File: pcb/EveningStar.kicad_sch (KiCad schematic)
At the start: 20 parts, among them J1 Conn_01x03_Pin, Q1 IRLL014NTRPBF, U1 74HC132, U2 ISO6721RBD

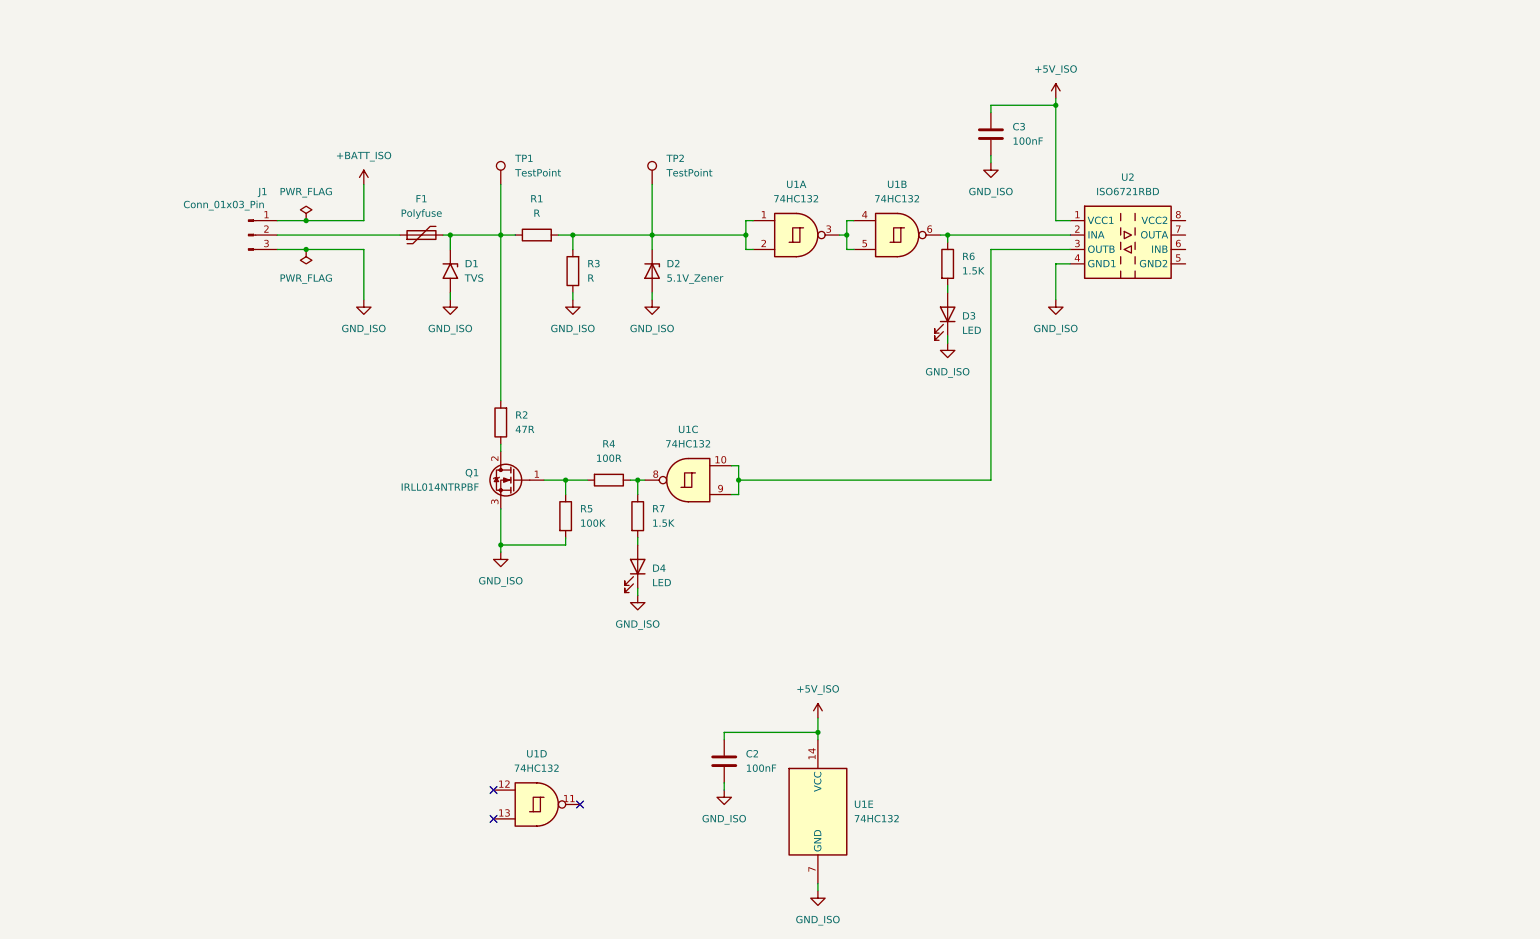
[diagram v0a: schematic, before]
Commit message: feat: implement more of the meterbus side isolated circuit
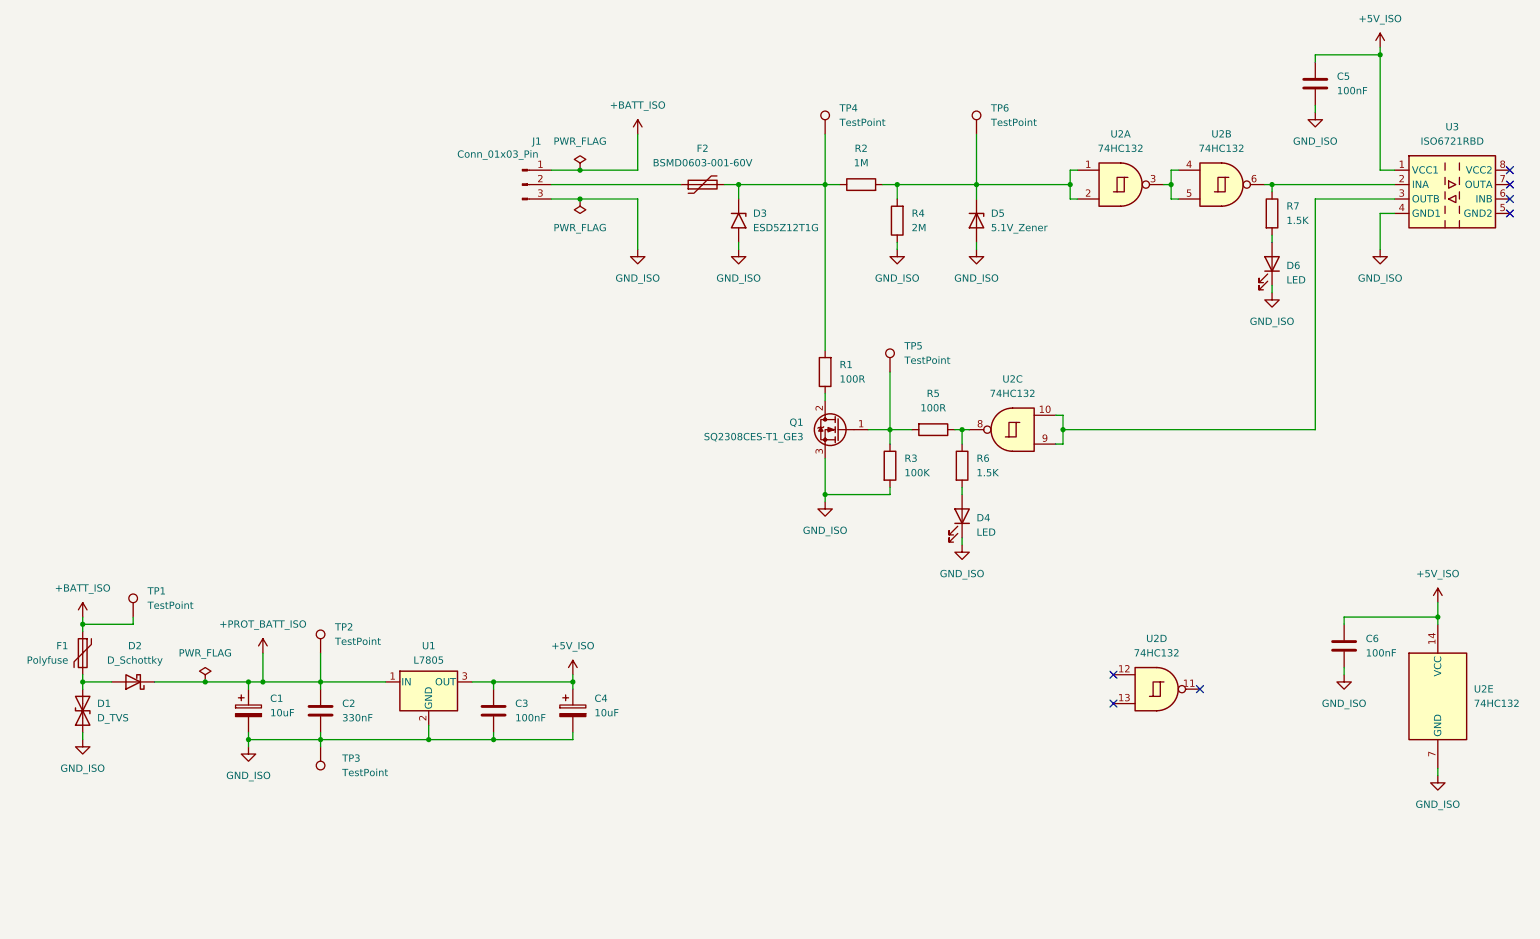
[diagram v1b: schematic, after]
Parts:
- added C1, C4: 10uF, symbol Device:C_Polarized
- added C2: 330nF, symbol Device:C
- added C3: 100nF, symbol Device:C
- added D1: D_TVS, symbol Device:D_TVS
- added D2: D_Schottky, symbol Device:D_Schottky
- added F1: Polyfuse, symbol Device:Polyfuse
- added TP1, TP2, TP3, TP5: TestPoint, symbol Connector:TestPoint
- added U1: L7805, symbol Regulator_Linear:L7805
- D3: renamed from D1; value TVS -> ESD5Z12T1G; footprint Diode_SMD:D_SMB -> Diode_SMD:D_SOD-523
- F2: renamed from F1; value Polyfuse -> BSMD0603-001-60V; footprint (none) -> Fuse:Fuse_0603_1608Metric_Pad1.05x0.95mm_HandSolder
- Q1: value IRLL014NTRPBF -> SQ2308CES-T1_GE3; footprint Package_TO_SOT_SMD:SOT-223-3_TabPin2 -> Package_TO_SOT_SMD:SOT-23
- R1: renamed from R2; value 47R -> 100R
- R2: renamed from R1; value R -> 1M
- R4: renamed from R3; value R -> 2M
- renumbered C3 to C5, C2 to C6, D2 to D5, D3 to D6, R5 to R3, R4 to R5, R7 to R6, R6 to R7, TP1 to TP4, TP2 to TP6, U1 to U2, U2 to U3
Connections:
- net +5V_ISO: now also C3.1, C4.1, U1.3 (OUT)
- net +BATT_ISO: now also F1.1, TP1.1
- net GND_ISO: now also C1.2, C2.2, C3.2, C4.2, D1.1 (A1), TP3.1, U1.2 (GND)
- net at Q1.1 (G), R3.1, R5.2: now also TP5.1
- new net: D1.2 (A2), D2.2 (A), F1.2
- new net +PROT_BATT_ISO: C1.1, C2.1, D2.1 (K), TP2.1, U1.1 (IN)
- no-connect marks 3 -> 7
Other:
- moved on the sheet: C5, C6, D3, D4, D5, D6, F2, J1, Q1, R1, R2, R3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

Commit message: feat: add 3.3V PSU
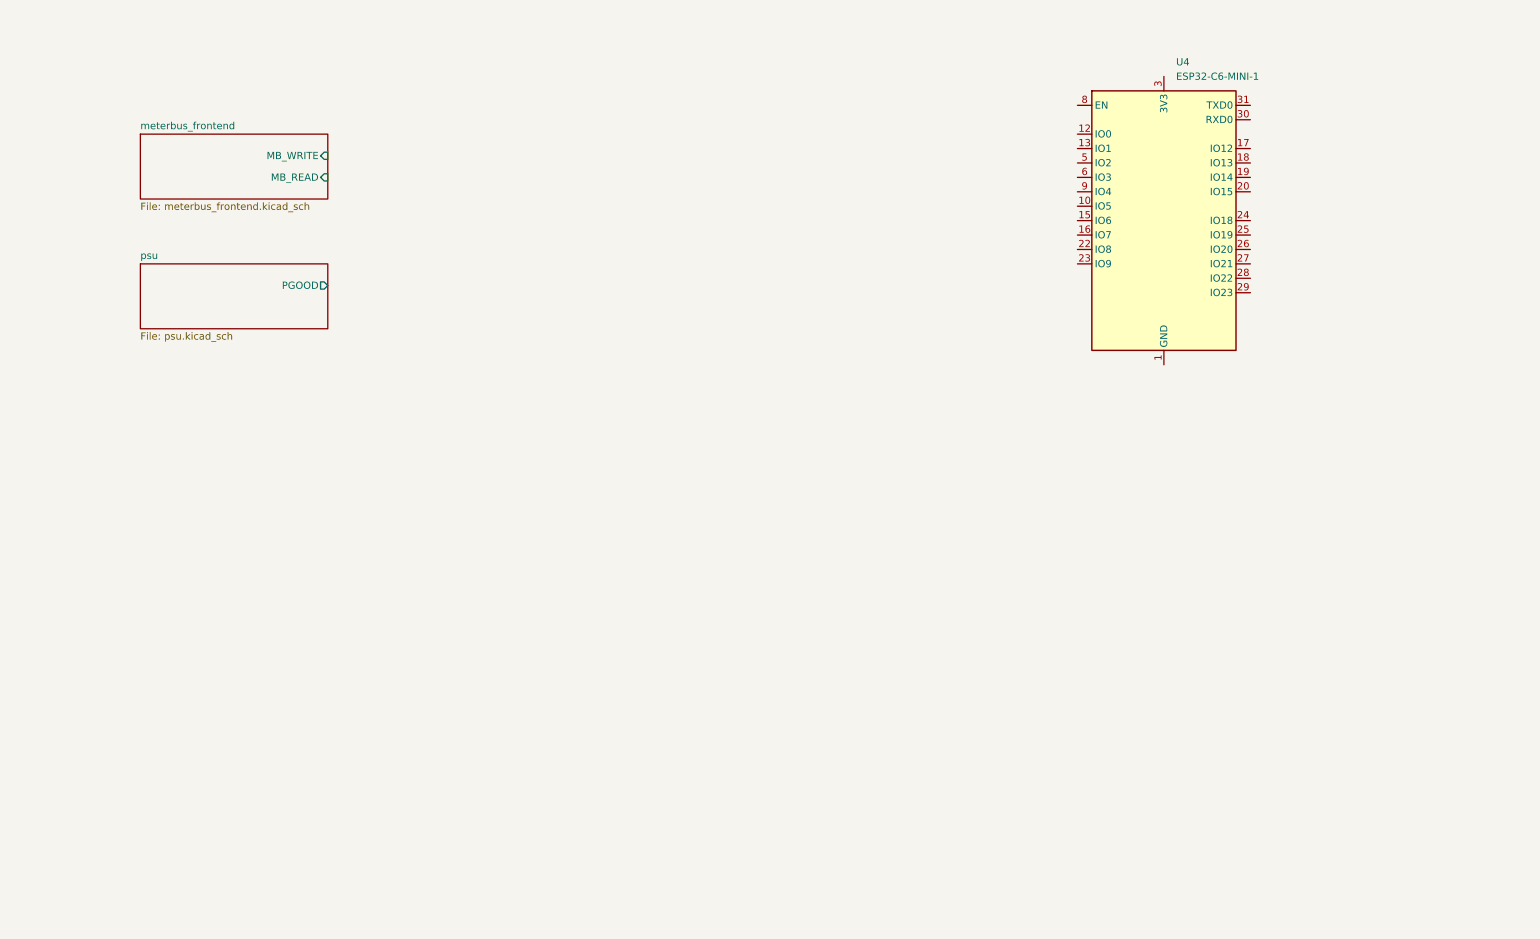
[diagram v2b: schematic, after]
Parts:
- removed C1, C4: 10uF, symbol Device:C_Polarized
- removed C2: 330nF, symbol Device:C
- removed C3, C5, C6: 100nF, symbol Device:C
- removed D1: D_TVS, symbol Device:D_TVS
- removed D2: D_Schottky, symbol Device:D_Schottky
- removed D3: ESD5Z12T1G, Diode_SMD:D_SOD-523, symbol Diode:SM6T15A
- removed D4, D6: LED, symbol Device:LED
- removed D5: 5.1V_Zener, symbol Device:D_Zener
- removed F1: Polyfuse, symbol Device:Polyfuse
- removed F2: BSMD0603-001-60V, Fuse:Fuse_0603_1608Metric_Pad1.05x0.95mm_HandSolder, symbol Device:Polyfuse
- removed J1: Conn_01x03_Pin, symbol Connector:Conn_01x03_Pin
- removed Q1: SQ2308CES-T1_GE3, Package_TO_SOT_SMD:SOT-23, symbol custom_symbols:IRLL014NTRPBF
- removed R1, R5: 100R, symbol Device:R
- removed R2: 1M, symbol Device:R
- removed R3: 100K, symbol Device:R
- removed R4: 2M, symbol Device:R
- removed R6, R7: 1.5K, symbol Device:R
- removed TP1, TP2, TP3, TP4, TP5, TP6: TestPoint, symbol Connector:TestPoint
- removed U1: L7805, symbol Regulator_Linear:L7805
- removed U2: 74HC132, symbol custom_symbols:74HC132
- removed U3: ISO6721RBD, Package_SO:SOIC-8_3.9x4.9mm_P1.27mm, symbol Isolator:ISO6721RBD
- added U4: ESP32-C6-MINI-1, RF_Module:ESP32-C6-MINI-1, symbol RF_Module:ESP32-C6-MINI-1
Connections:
- new net: U4.1 (GND), U4.11 (GND), U4.14 (GND), U4.2 (GND), U4.36 (GND), U4.37 (GND), U4.38 (GND), U4.39 (GND), U4.40 (GND), U4.41 (GND), U4.42 (GND), U4.43 (GND), U4.44 (GND), U4.45 (GND), U4.46 (GND), U4.47 (GND), U4.48 (GND), U4.49 (GND), U4.50 (GND), U4.51 (GND), U4.52 (GND), U4.53 (GND)
- no-connect marks 7 -> 0
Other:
- added sheet meterbus_frontend (meterbus_frontend.kicad_sch)
- added sheet psu (psu.kicad_sch)

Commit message: feat: add MCU sheet with USB, reset and programming circuitry
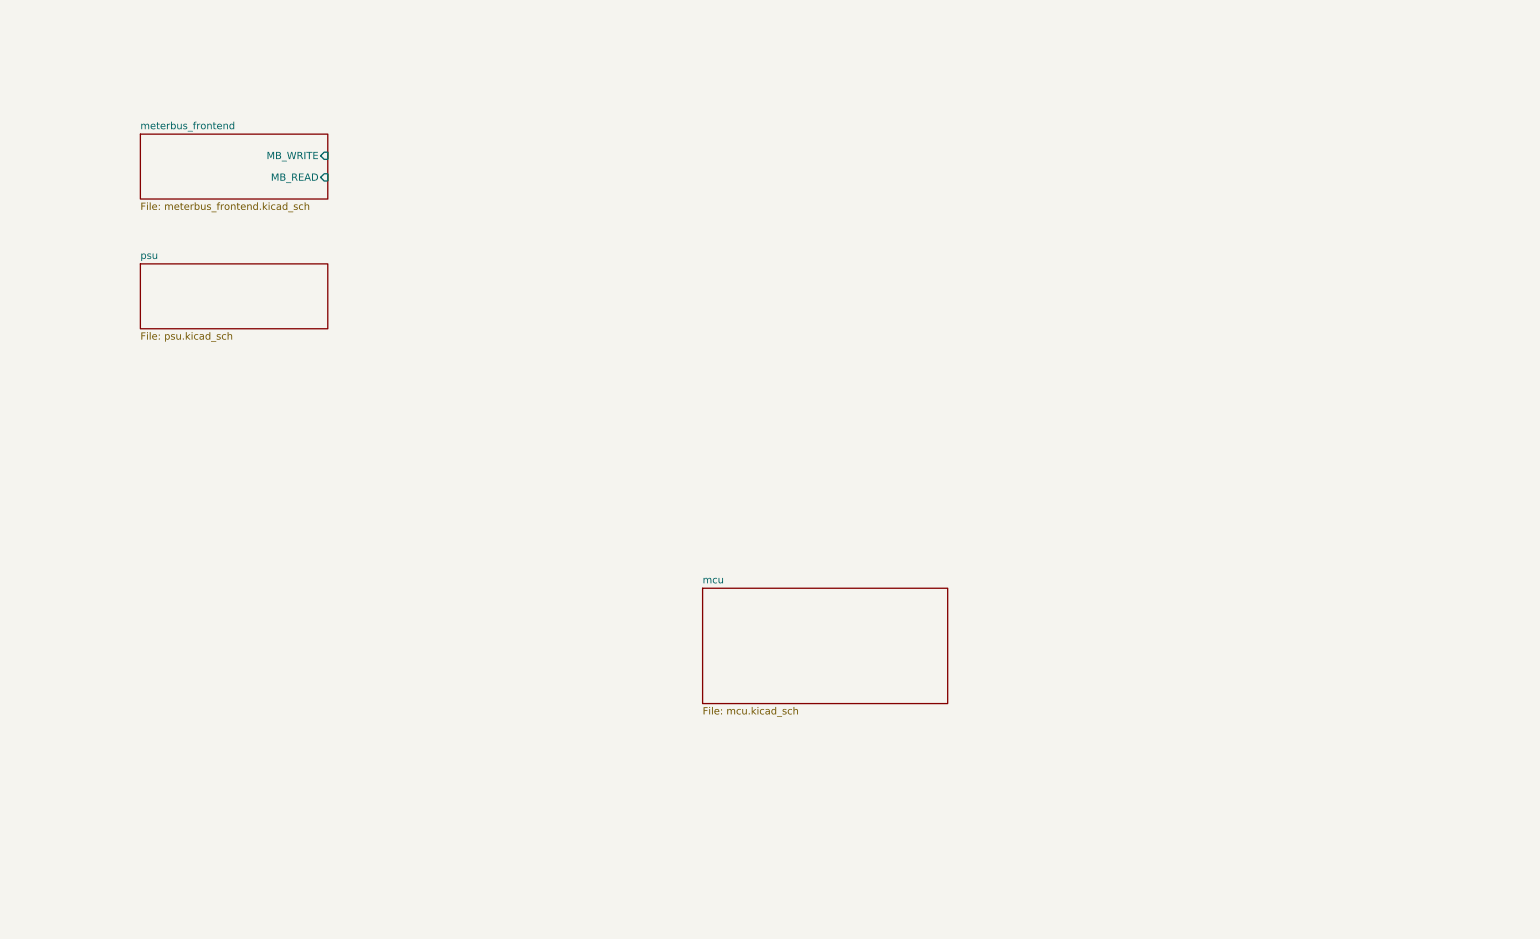
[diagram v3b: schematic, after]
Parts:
- removed U4: ESP32-C6-MINI-1, RF_Module:ESP32-C6-MINI-1, symbol RF_Module:ESP32-C6-MINI-1
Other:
- added sheet mcu (mcu.kicad_sch)
- sheet psu ports: added none; removed PGOOD
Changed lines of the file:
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@@
 	(generator_version "10.0")
 	(paper "A4")
-	(symbol
-		(lib_id "RF_Module:ESP32-C6-MINI-1")
-		(at 215.9 52.07 0)
-		(unit 1)
-		(body_style 1)
-		(exclude_from_sim no)
-		(in_bom yes)
-		(on_board yes)
-		(in_pos_files yes)
-		(dnp no)
-		(fields_autoplaced yes)
-		(property "Reference" "U4"
-			(at 218.0433 24.13 0)
-			(show_name no)
-			(do_not_autoplace no)
-			(effects
-				(font
-					(size 1.27 1.27)
-				)
-				(justify left)
-			)
-		)
-		(property "Value" "ESP32-C6-MINI-1"
-			(at 218.0433 26.67 0)
-			(show_name no)
-			(do_not_autoplace no)
-			(effects
-				(font
-					(size 1.27 1.27)
-				)
-				(justify left)
-			)
-		)
-		(property "Footprint" "RF_Module:ESP32-C6-MINI-1"
-			(at 233.68 77.47 0)
-			(hide yes)
-			(show_name no)
-			(do_not_autoplace no)
-			(effects
-				(font
-					(size 1.27 1.27)
-				)
-			)
-		)
-		(property "Datasheet" "https://www.espressif.com/sites/default/files/documentation/esp32-c6-mini-1_mini-1u_datasheet_en.pdf"
-			(at 215.9 15.24 0)
-			(hide yes)
-			(show_name no)
-			(do_not_autoplace no)
-			(effects
-				(font
-					(size 1.27 1.27)
-				)
-			)
-		)
-		(property "Description" "RF Module, ESP32-C6 SoC, Wi-Fi 802.11b/g/n/ax, Bluetooth, BLE, Zigbee, Thread, 32-bit, 3.3V, SMD, onboard antenna"
-			(at 215.9 12.7 0)
-			(hide yes)
-			(show_name no)
-			(do_not_autoplace no)
-			(effects
-				(font
-					(size 1.27 1.27)
-				)
-			)
-		)
-		(pin "35"
-		)
-		(pin "38"
-		)
-		(pin "10"
-		)
-		(pin "24"
-		)
-		(pin "27"
-		)
-		(pin "25"
-		)
-		(pin "28"
-		)
-		(pin "26"
-		)
-		(pin "30"
-		)
-		(pin "23"
-		)
-		(pin "44"
-		)
-		(pin "47"
-		)
-		(pin "14"
-		)
-		(pin "7"
-		)
-		(pin "15"
-		)
-		(pin "9"
-		)
-		(pin "11"
-		)
-		(pin "19"
-		)
-		(pin "50"
-		)
-		(pin "42"
-		)
-		(pin "40"
-		)
-		(pin "45"
-		)
-		(pin "29"
-		)
-		(pin "52"
-		)
-		(pin "43"
-		)
-		(pin "48"
-		)
-		(pin "46"
-		)
-		(pin "34"
-		)
-		(pin "49"
-		)
-		(pin "20"
-		)
-		(pin "53"
-		)
-		(pin "36"
-		)
-		(pin "51"
-		)
-		(pin "39"
-		)
-		(pin "37"
-		)
-		(pin "18"
-		)
-		(pin "21"
-		)
-		(pin "22"
-		)
-		(pin "41"
-		)
-		(pin "8"
-		)
-		(pin "16"
-		)
-		(pin "12"
-		)
-		(pin "13"
-		)
-		(pin "32"
-		)
-		(pin "17"
-		)
-		(pin "33"
-		)
-		(pin "31"
-		)
-		(pin "1"
-		)
-		(pin "6"
-		)
-		(pin "5"
-		)
-		(pin "4"
-		)
-		(pin "3"
-		)
-		(pin "2"
-		)
-		(instances
-			(project "EveningStar"
-				(path "/4c61f5a2-f8d4-462a-9bc3-d74437d30372"
-					(reference "U4")
-					(unit 1)
-				)
-			)
-		)
-	)
 	(sheet
 		(at 35.56 36.83)
@@
 			)
 		)
-		(pin "PGOOD" output
-			(at 68.58 63.5 0)
-			(effects
-				(font
-					(size 1.27 1.27)
-				)
-				(justify right)
-			)
-		)
 		(instances
 			(project "EveningStar"
@@
 				)
 			)
+		)
+	)
+	(sheet
+		(at 134.62 116.84)
+		(size 43.18 20.32)
+		(exclude_from_sim no)
+		(in_bom yes)
+		(on_board yes)
+		(dnp no)
+		(fields_autoplaced yes)
+		(stroke
+			(width 0.1524)
+			(type solid)
+		)
+		(fill
+			(color 0 0 0 0)
+		)
+		(property "Sheetname" "mcu"
+			(at 134.62 116.1284 0)
+			(show_name no)
+			(do_not_autoplace no)
+			(effects
+				(font
+					(size 1.27 1.27)
+				)
+				(justify left bottom)
+			)
+		)
+		(property "Sheetfile" "mcu.kicad_sch"
+			(at 134.62 137.7446 0)
+			(show_name no)
+			(do_not_autoplace no)
+			(effects
+				(font
+					(size 1.27 1.27)
+				)
+				(justify left top)
+			)
+		)
+		(instances
+			(project "EveningStar"
+				(path "/4c61f5a2-f8d4-462a-9bc3-d74437d30372"
+					(page "4")
+				)
+			)
